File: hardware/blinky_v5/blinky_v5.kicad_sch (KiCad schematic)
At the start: 237 parts, among them J1 RJ45, J10 Conn_01x04, J11 Conn_01x08, J12 Conn_01x06, J2 Conn_01x06_Pin, J3 Conn_01x05_Pin, J5 Conn_01x06_Pin, J6 Conn_01x04_Pin, J7 Conn_01x04_Pin, J8 Conn_01x02, J9 Conn_02x10_Odd_Even, Q1 2N7002, Q2 2N7002, Q3 2N7002, Q4 2N7002, Q5 2N7002, Q6 2N7002, Q7 2N7002, Q8 2N7002, U1 ADA4807-1, U10 STM32F405RGTx, U11 AMS1117-3.3, U12 BA50DD0WHFP-TR, U13 M24C02-RMN, U2 SN74LVC1G14DBV, U3 SN74LVC1G14DBV, U4 ADA4807-1, U5 ADA4807-1, U6 TLV3603DCKR, U7 SN74LVC1G14DBV, U8 TLV3603DCKR, U9 L78L05_SOT89, X1 GTXO-14V (2.048MHz), X2 GTXO-14V (2.048MHz), Y1 AOCJY4A-10.000MHZ-SW, Y2 16MHz

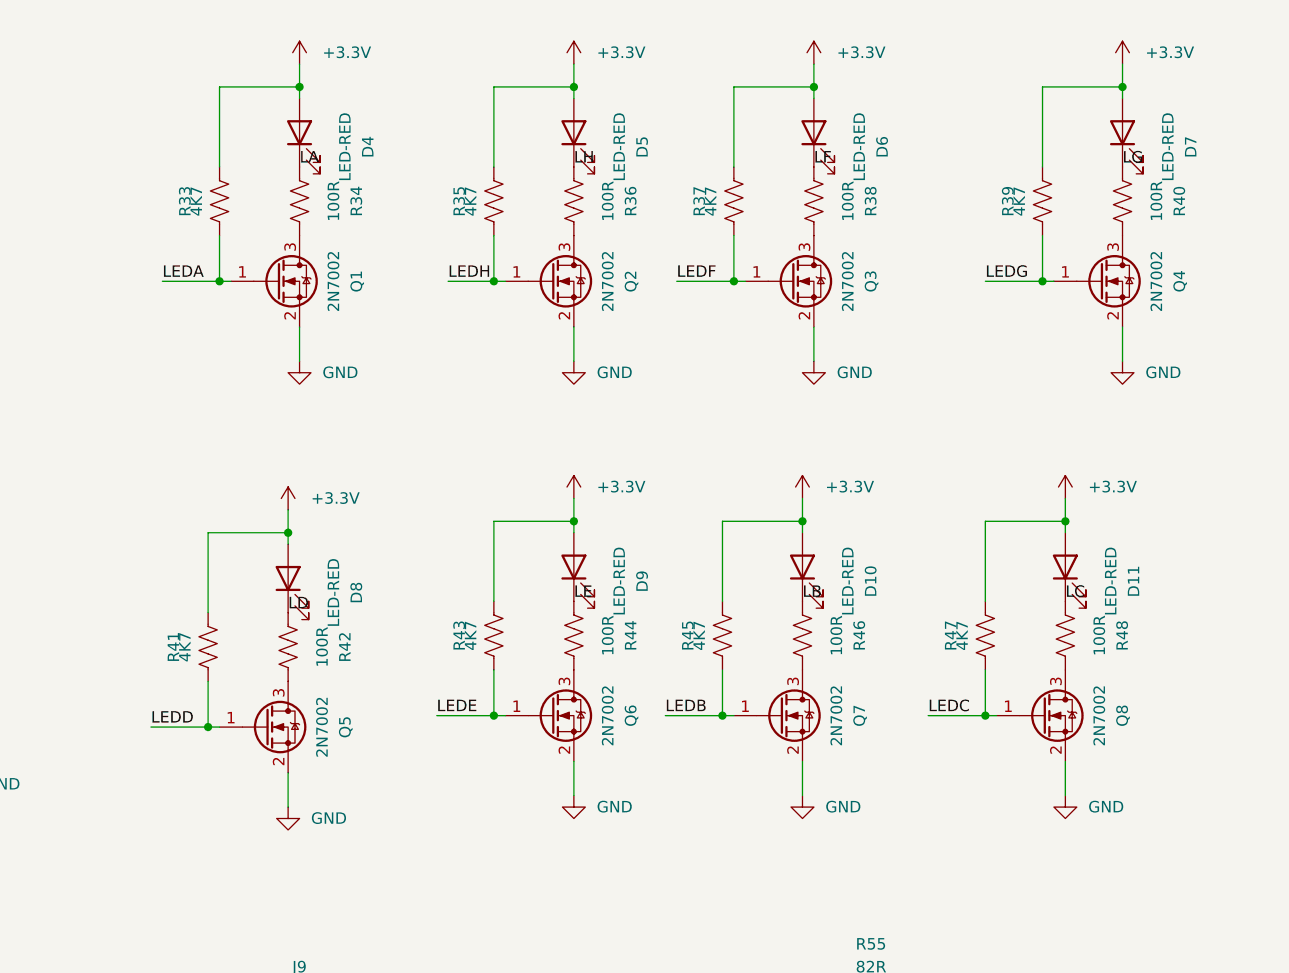
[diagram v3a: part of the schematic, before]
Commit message: move LED resistors to pull down from pull up
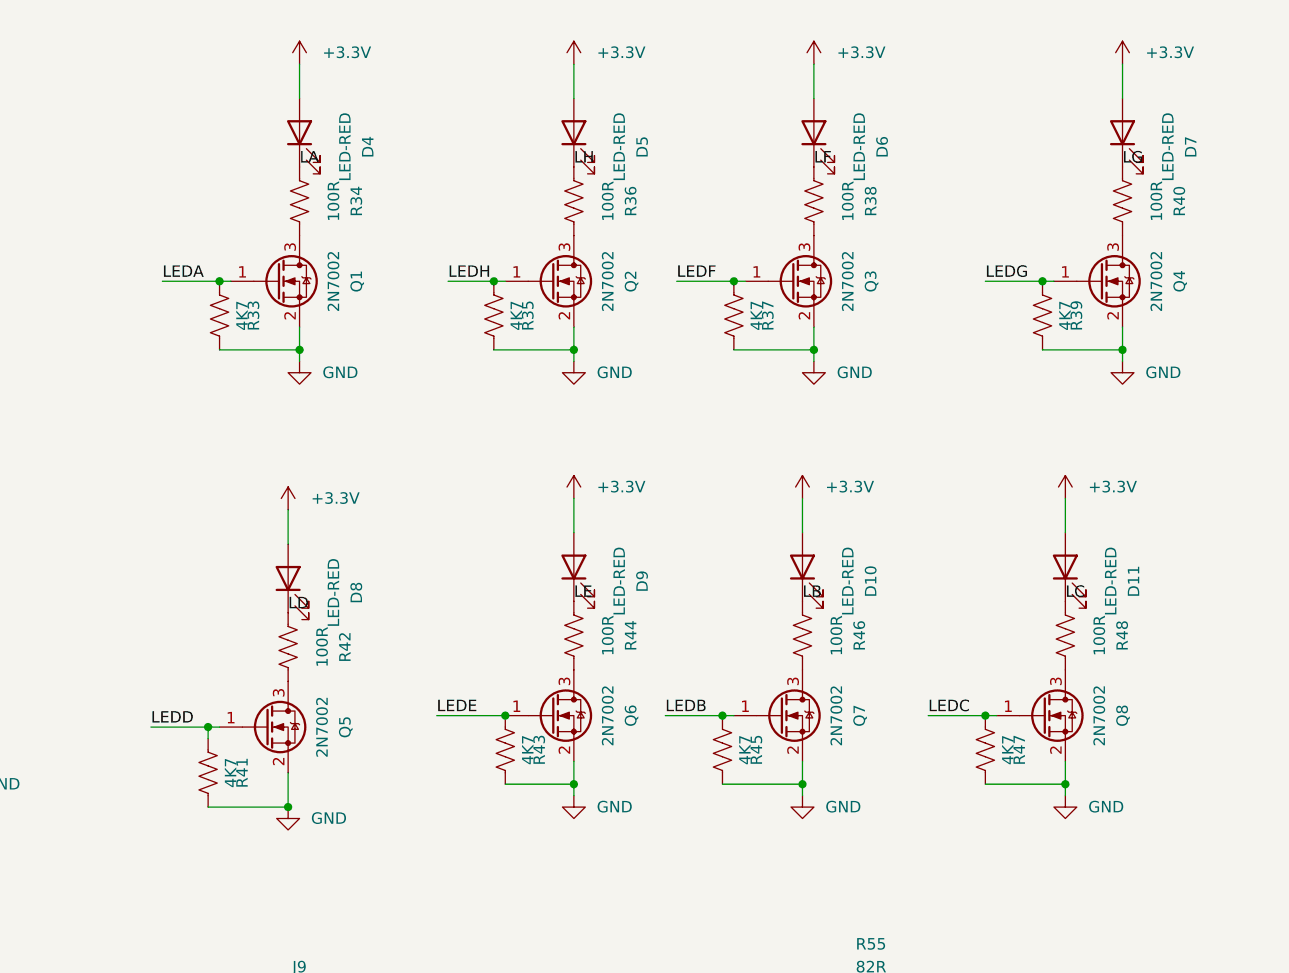
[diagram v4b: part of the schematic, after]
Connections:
- net +3.3V: no longer R33.1, R35.1, R37.1, R39.1, R41.1, R43.1, R45.1, R47.1
- net GND: now also R33.1, R35.1, R37.1, R39.1, R41.1, R43.1, R45.1, R47.1
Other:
- moved on the sheet: R33, R35, R37, R39, R41, R43, R45, R47

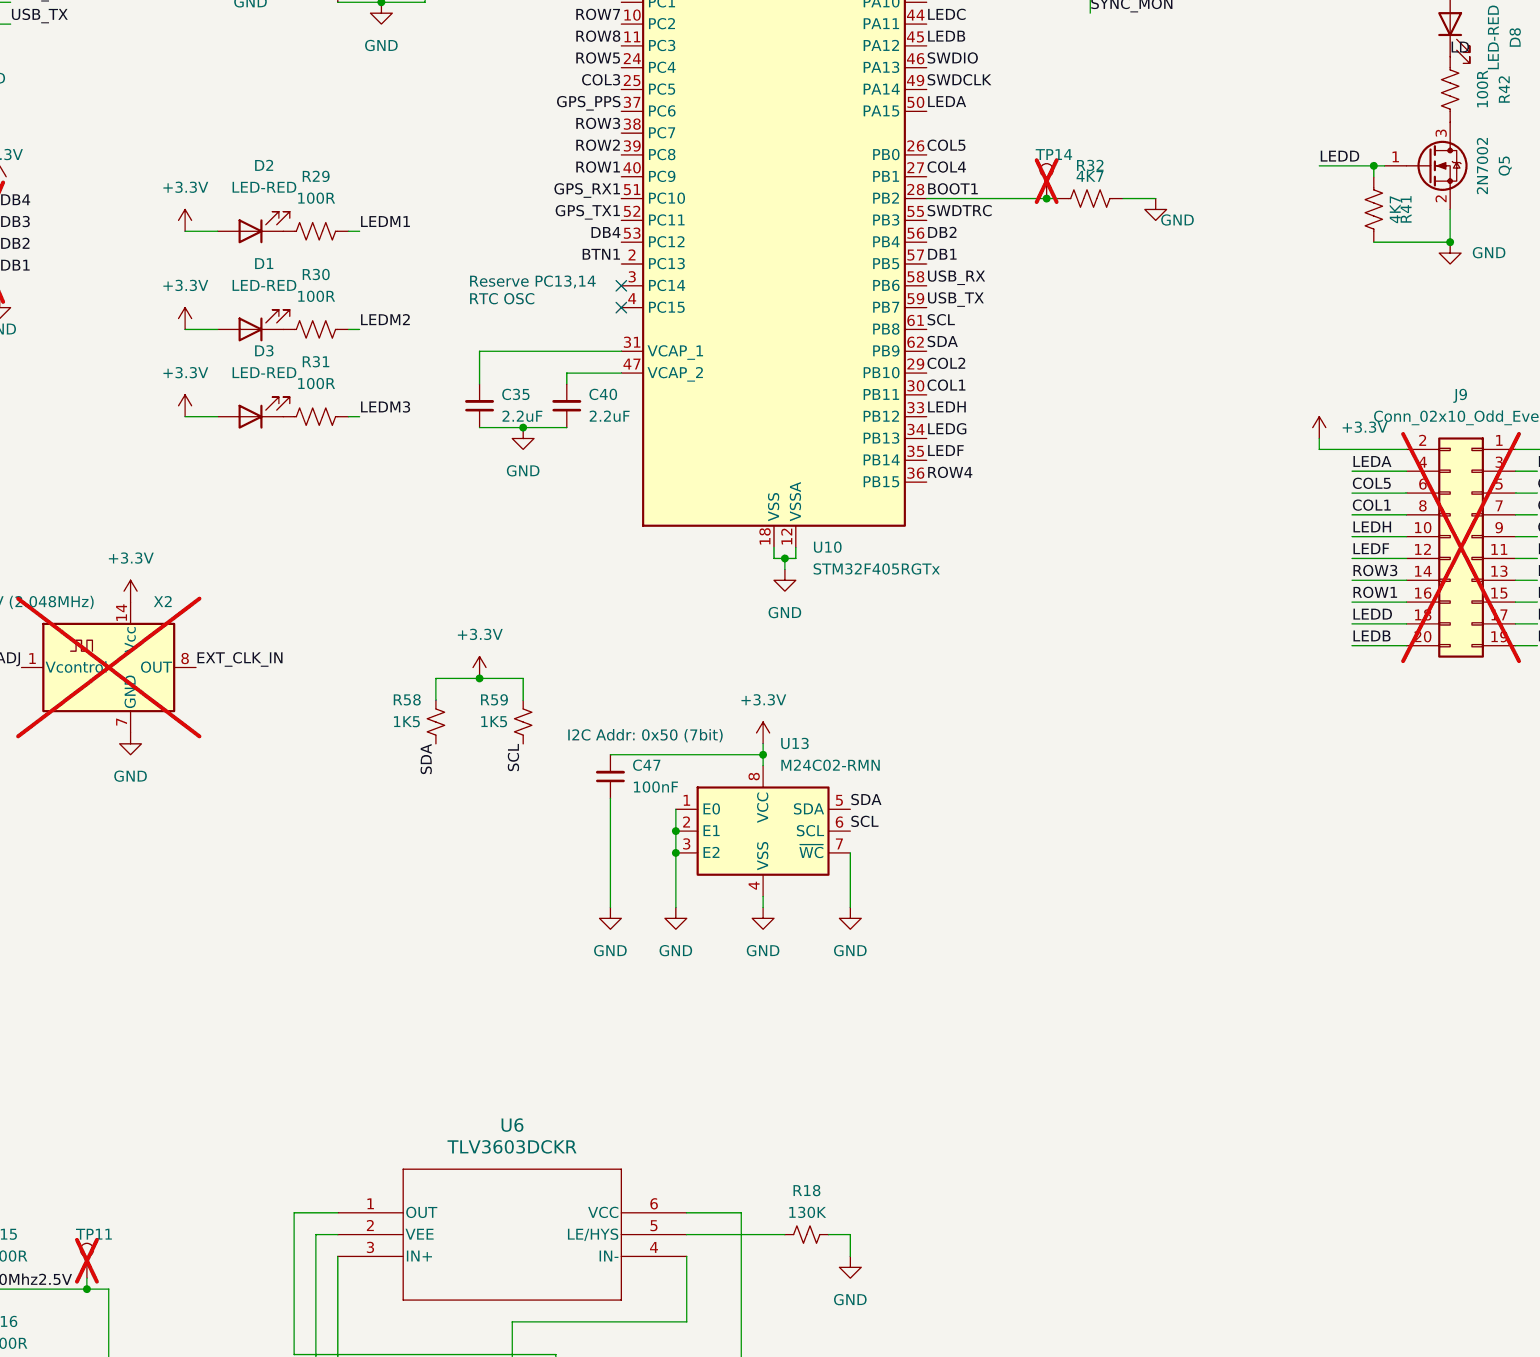
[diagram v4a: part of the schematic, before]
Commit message: update to have FET drivers for some of status LEDs
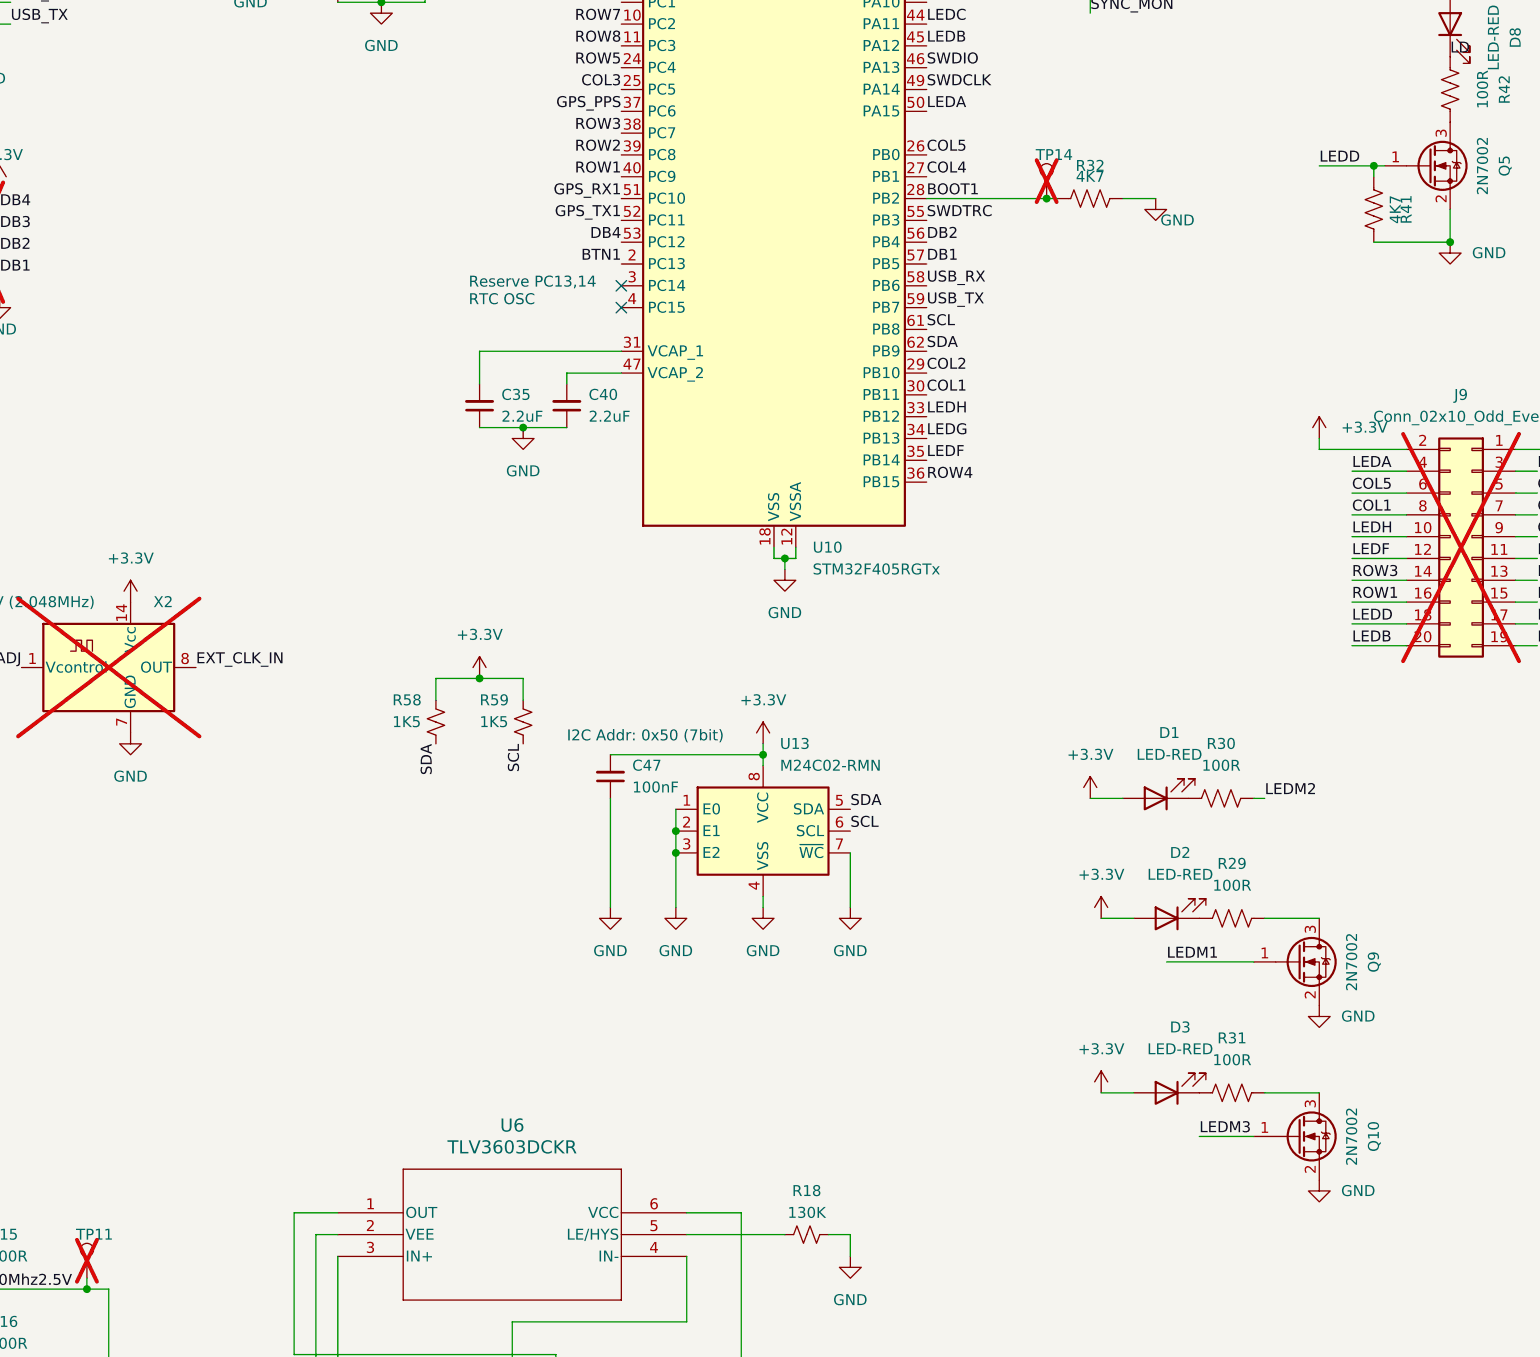
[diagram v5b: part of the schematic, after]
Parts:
- added Q10, Q9: 2N7002, Package_TO_SOT_SMD:SOT-23, symbol Transistor_FET:2N7002
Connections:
- net GND: now also Q10.2 (S), Q9.2 (S)
- net LEDM1: now also Q9.1 (G); no longer R29.2
- net LEDM3: now also Q10.1 (G); no longer R31.2
- new net: Q10.3 (D), R31.2
- new net: Q9.3 (D), R29.2
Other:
- moved on the sheet: D1, D2, D3, R29, R30, R31
